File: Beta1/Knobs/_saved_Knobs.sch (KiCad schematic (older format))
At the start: 34 parts, among them U1000 MCP3008T-I/SL, U2 MCP3008T-I/SL

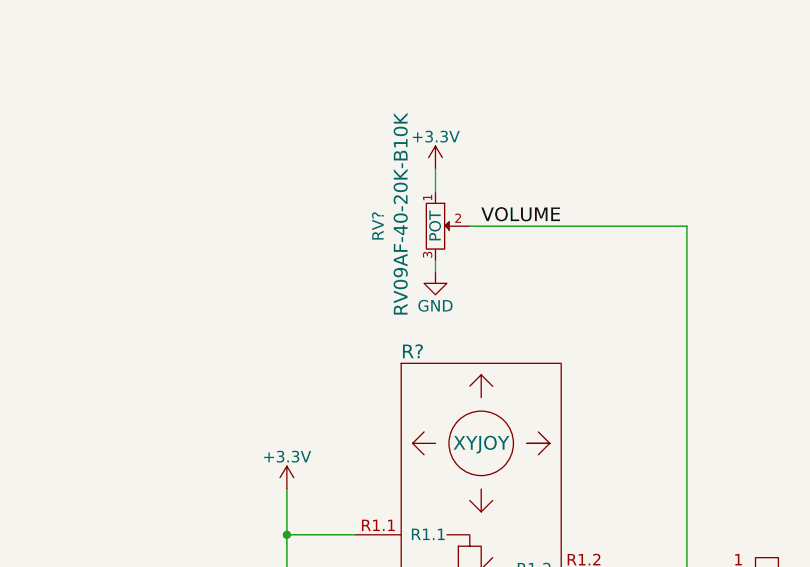
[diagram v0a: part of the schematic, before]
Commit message: Added volume knob + XY Joy to Knobs 16 CH Board.
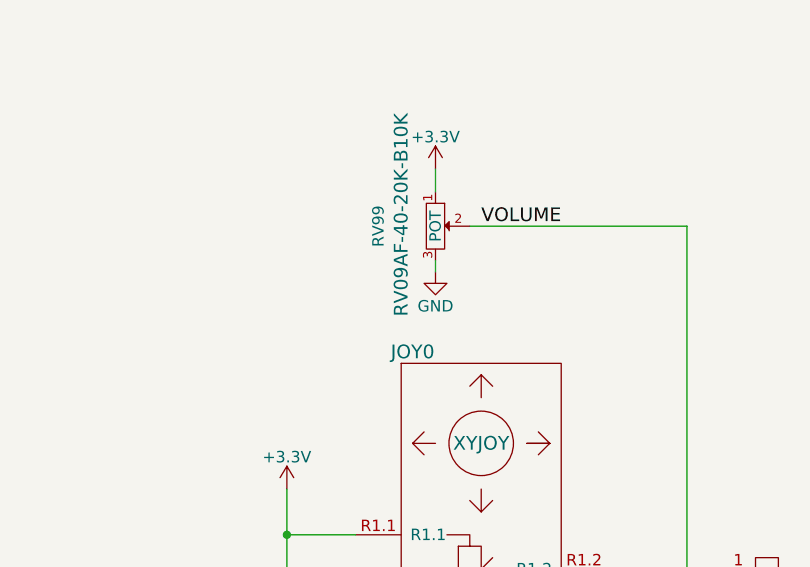
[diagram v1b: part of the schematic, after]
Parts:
- JOY0: renamed from R?; footprint (none) -> Liberry:XY_JOY_254TA103B50B
- gave numbers to parts that had none: 1
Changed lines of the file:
@@
 $EndComp
 $Comp
-L XYJOY R?
+L XYJOY JOY0
 U 1 1 5880F7E5
 P 4500 8050
-F 0 "R?" H 4200 9000 60  0000 C CNN
+F 0 "JOY0" H 4200 9000 60  0000 C CNN
 F 1 "XYJOY" H 4500 8600 60  0000 C CNN
-F 2 "" H 4500 8600 60  0001 C CNN
+F 2 "Liberry:XY_JOY_254TA103B50B" H 4500 8600 60  0001 C CNN
 F 3 "" H 4500 8600 60  0001 C CNN
 	1    4500 8050
@@
 $EndComp
 $Comp
-L +3.3V #PWR?
+L +3.3V #PWR039
 U 1 1 5880F86D
 P 3650 7700
-F 0 "#PWR?" H 3650 7550 50  0001 C CNN
+F 0 "#PWR039" H 3650 7550 50  0001 C CNN
 F 1 "+3.3V" H 3650 7840 50  0000 C CNN
 F 2 "" H 3650 7700 50  0000 C CNN
@@
 $EndComp
 $Comp
-L GND #PWR?
+L GND #PWR040
 U 1 1 5880F8DB
 P 3750 9150
-F 0 "#PWR?" H 3750 8900 50  0001 C CNN
+F 0 "#PWR040" H 3750 8900 50  0001 C CNN
 F 1 "GND" H 3750 9000 50  0000 C CNN
 F 2 "" H 3750 9150 50  0000 C CNN
@@
 Connection ~ 3750 8950
 $Comp
-L POT RV?
+L POT RV99
 U 1 1 58810DA5
 P 4300 6550
-F 0 "RV?" H 4300 6300 50  0000 C CNN
+F 0 "RV99" H 4300 6300 50  0000 C CNN
 F 1 "POT" H 4300 6550 50  0000 C CNN
 F 2 "Liberry:RV09AF-40-20K-B10K" H 4300 6550 50  0001 C CNN
@@
 $EndComp
 $Comp
-L GND #PWR?
+L GND #PWR041
 U 1 1 58810DAB
 P 4300 6750
-F 0 "#PWR?" H 4300 6500 50  0001 C CNN
+F 0 "#PWR041" H 4300 6500 50  0001 C CNN
 F 1 "GND" H 4300 6600 50  0000 C CNN
 F 2 "" H 4300 6750 50  0000 C CNN
@@
 $EndComp
 $Comp
-L +3.3V #PWR?
+L +3.3V #PWR042
 U 1 1 58810DB1
 P 4300 6300
-F 0 "#PWR?" H 4300 6150 50  0001 C CNN
+F 0 "#PWR042" H 4300 6150 50  0001 C CNN
 F 1 "+3.3V" H 4300 6440 50  0000 C CNN
 F 2 "" H 4300 6300 50  0000 C CNN
